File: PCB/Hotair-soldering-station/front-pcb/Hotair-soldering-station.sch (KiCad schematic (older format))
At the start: 54 parts, among them J1 fan_reg_pot, J2 main-board-conn, J3 hot_on, J4 solder_on, Q1 BC817, Q10 BC807, Q11 BC807, Q12 BC807, Q13 BC807, Q14 BC807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

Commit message: add heater controll circuit, add sch block structure
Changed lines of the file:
@@
 U 1 1 5FAAAC4E
 P 5550 8125
-F 0 "R6" H 5480 8079 50  0000 R CNN
-F 1 "5k6" H 5480 8170 50  0000 R CNN
+F 0 "R6" V 5650 8175 50  0000 R CNN
+F 1 "5k6" V 5450 8200 50  0000 R CNN
 F 2 "Capacitors:0805" V 5480 8125 50  0001 C CNN
 F 3 "~" H 5550 8125 50  0001 C CNN

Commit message: main schematic update, front pcb routing
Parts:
- SW1: value SW_Push -> HOTAIR_UP
- SW2: value SW_Push -> HOTAIR_DOWN
- SW3: value SW_Push -> SIRON_UP
- SW4: value SW_Push -> SIRON_DOWN
- U3, U4: symbol My-Lib:3-dig-7-seg-display-common-anode -> Hotair-soldering-station-rescue:3-dig-7-seg-display-common-anode-My-Lib
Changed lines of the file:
@@
 P 12125 5725
 F 0 "SW1" H 11925 5775 50  0000 C CNN
-F 1 "SW_Push" H 12125 5919 50  0001 C CNN
+F 1 "HOTAIR_UP" H 12125 5919 50  0001 C CNN
 F 2 "My-Footprints:push_button_12mm" H 12125 5925 50  0001 C CNN
 F 3 "~" H 12125 5925 50  0001 C CNN
@@
 P 12125 5925
 F 0 "SW2" H 11925 5975 50  0000 C CNN
-F 1 "SW_Push" H 12125 6119 50  0001 C CNN
+F 1 "HOTAIR_DOWN" H 12125 6119 50  0001 C CNN
 F 2 "My-Footprints:push_button_12mm" H 12125 6125 50  0001 C CNN
 F 3 "~" H 12125 6125 50  0001 C CNN
@@
 P 12175 7125
 F 0 "SW3" H 11975 7175 50  0000 C CNN
-F 1 "SW_Push" H 12175 7319 50  0001 C CNN
+F 1 "SIRON_UP" H 12175 7319 50  0001 C CNN
 F 2 "My-Footprints:push_button_12mm" H 12175 7325 50  0001 C CNN
 F 3 "~" H 12175 7325 50  0001 C CNN
@@
 P 12175 7325
 F 0 "SW4" H 11975 7375 50  0000 C CNN
-F 1 "SW_Push" H 12175 7519 50  0001 C CNN
+F 1 "SIRON_DOWN" H 12175 7519 50  0001 C CNN
 F 2 "My-Footprints:push_button_12mm" H 12175 7525 50  0001 C CNN
 F 3 "~" H 12175 7525 50  0001 C CNN
@@
 	11425 4725 11425 8125
 $Comp
-L My-Lib:3-dig-7-seg-display-common-anode U4
+L Hotair-soldering-station-rescue:3-dig-7-seg-display-common-anode-My-Lib U4
 U 1 1 5F79E7AA
 P 8200 7975
@@
 	8950 5525 9650 5525
 $Comp
-L My-Lib:3-dig-7-seg-display-common-anode U3
+L Hotair-soldering-station-rescue:3-dig-7-seg-display-common-anode-My-Lib U3
 U 1 1 5F79D382
 P 8200 5475

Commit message: routing progress
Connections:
- net SEG_B: now reaches U1.1 (QB)
- net SEG_B: now also R7.1; no longer R2.1
- net SEG_A: now reaches U1.15 (QA)
- net SEG_A: now also R8.1; no longer R1.1
- net SEG_C: now reaches U1.2 (QC)
- net SEG_C: now also R6.1; no longer R3.1
- net SEG_D: now reaches U1.3 (QD)
- net SEG_D: now also R5.1; no longer R4.1
- net SEG_E: now reaches U1.4 (QE)
- net SEG_E: now also R4.1; no longer R5.1
- net HOTAIR_DIG3: now reaches U1.5 (QF)
- net HOTAIR_DIG3: now also R20.2; no longer R6.1
- net HOTAIR_DIG2: now reaches U1.6 (QG)
- net HOTAIR_DIG2: now also R19.2; no longer R7.1
- net HOTAIR_DIG1: now reaches U1.7 (QH)
- net HOTAIR_DIG1: now also R22.2; no longer R8.1
- net at U2.1 (QB): no longer R19.2
- net SEG_DP: now reaches U2.15 (QA)
- net SEG_DP: now also R1.1; no longer R20.2
- net SEG_G: now reaches U2.2 (QC)
- net SEG_G: now also R2.1; no longer R22.2
- net IRON_DIG1: now reaches U2.3 (QD)
- net IRON_DIG1: now also R21.2; no longer R18.2
- net IRON_DIG2: now reaches R17.2, U2.4 (QE)
- net IRON_DIG3: now reaches U2.5 (QF)
- net IRON_DIG3: now also R18.2; no longer R21.2
- new net SEG_F: R3.1
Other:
- moved on the sheet: R20, U1, U2

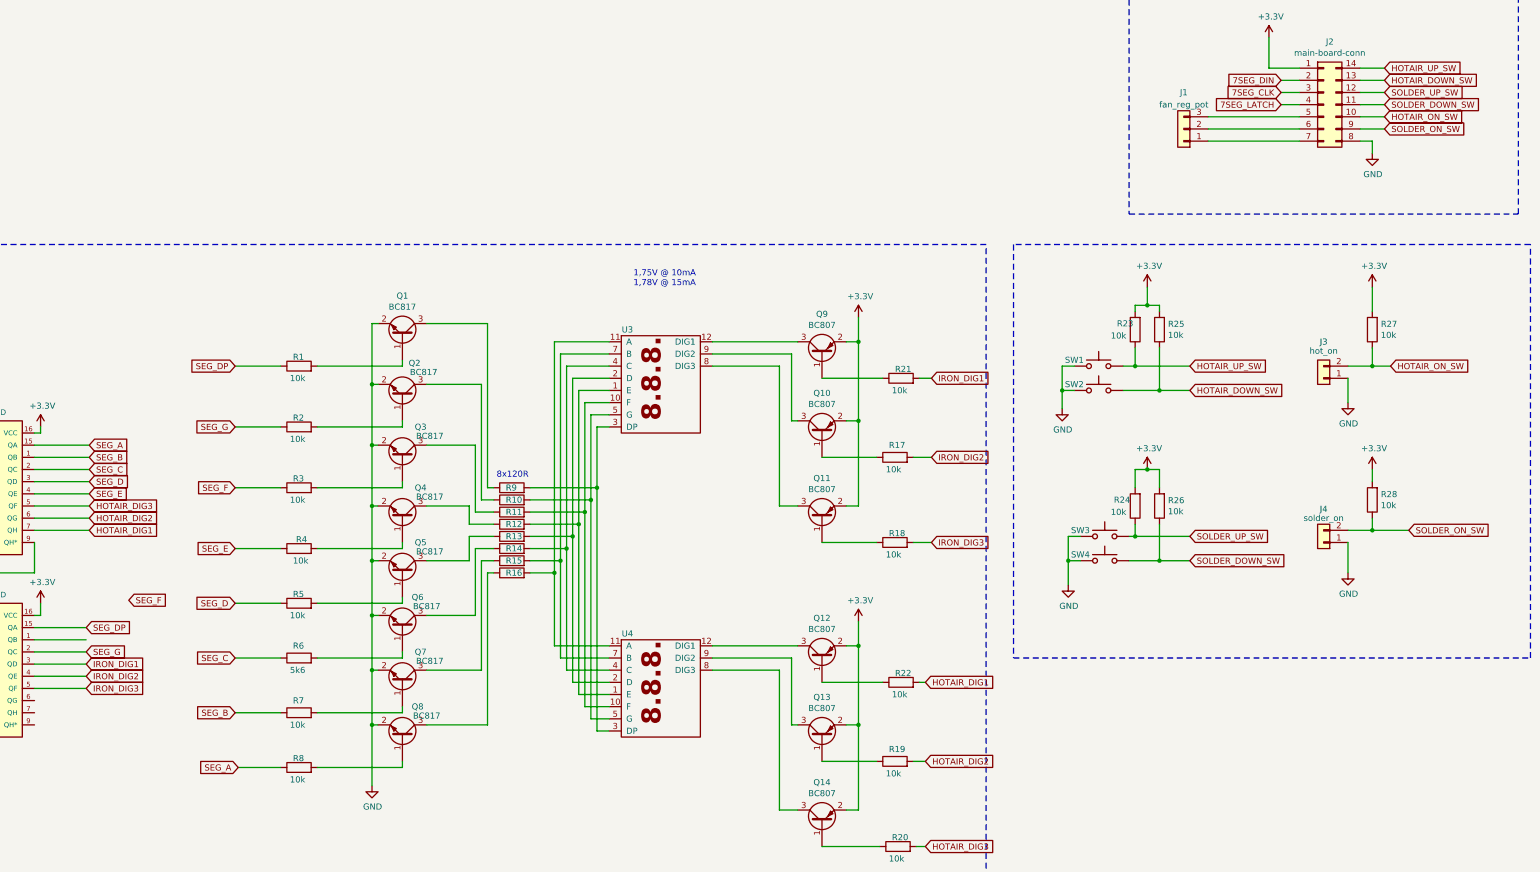
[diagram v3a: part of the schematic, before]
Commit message: add hot air fan buttons
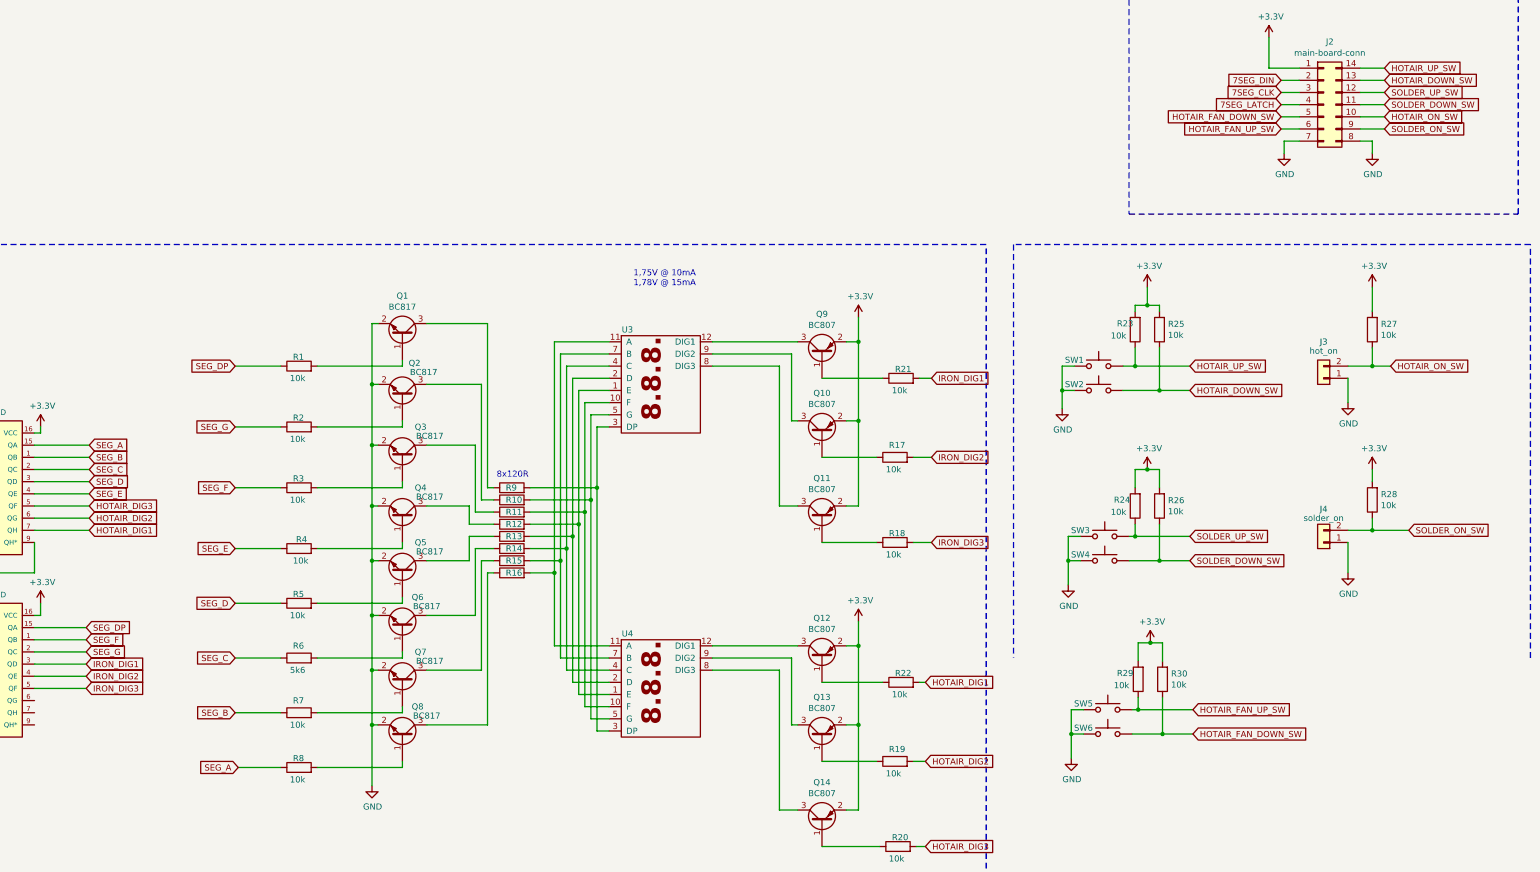
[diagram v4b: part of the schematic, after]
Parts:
- removed J1: fan_reg_pot, Connector_PinHeader_2.54mm:PinHeader_1x03_P2.54mm_Vertical, symbol Connector_Generic:Conn_01x03
- added R29, R30: 10k, Capacitors:0805, symbol Device:R
- added SW5: SIRON_UP, Switches:TACTILE_SWITCH_PTH_12MM, symbol Switch:SW_Push
- added SW6: SIRON_DOWN, Switches:TACTILE_SWITCH_PTH_12MM, symbol Switch:SW_Push
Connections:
- net +3V3: now also R29.2, R30.2
- net GND: now also J2.7 (Pin_7), SW5.1, SW6.1
- net SEG_F: now also U2.1 (QB)
- net HOTAIR_FAN_DOWN_SW: now reaches J2.5 (Pin_5)
- net HOTAIR_FAN_DOWN_SW: now also R30.1, SW6.2
- net HOTAIR_FAN_UP_SW: now reaches J2.6 (Pin_6)
- net HOTAIR_FAN_UP_SW: now also R29.1, SW5.2
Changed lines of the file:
@@
 SOLDER_ON_SW
-Wire Notes Line
-	11425 8125 15675 8125
 Wire Notes Line
 	15675 8125 15675 4725
@@
 Wire Wire Line
 	14275 3775 14475 3775
-$Comp
-L Connector_Generic:Conn_01x03 J1
-U 1 1 5F94CEDF
-P 12825 3775
-F 0 "J1" H 12825 3475 50  0000 C CNN
-F 1 "fan_reg_pot" H 12825 3575 50  0000 C CNN
-F 2 "Connector_PinHeader_2.54mm:PinHeader_1x03_P2.54mm_Vertical" H 12825 3775 50  0001 C CNN
-F 3 "~" H 12825 3775 50  0001 C CNN
-	1    12825 3775
-	-1   0    0    1
-$EndComp
-Wire Wire Line
-	13025 3675 13775 3675
-Wire Wire Line
-	13775 3775 13025 3775
-Wire Wire Line
-	13775 3875 13025 3875
 Wire Notes Line
 	12375 2475 12375 4475
@@
 Text GLabel 3825 6775 2    50   Input ~ 0
 SEG_E
-Text GLabel 4150 7650 2    50   Input ~ 0
+Text GLabel 3800 7975 2    50   Input ~ 0
 SEG_F
 Text GLabel 3800 8075 2    50   Input ~ 0
@@
 Text GLabel 10750 7175 2    50   Input ~ 0
 IRON_DIG3
+$Comp
+L Switch:SW_Push SW5
+U 1 1 5F8FF5F0
+P 12200 8550
+F 0 "SW5" H 12000 8600 50  0000 C CNN
+F 1 "SIRON_UP" H 12200 8744 50  0001 C CNN
+F 2 "Switches:TACTILE_SWITCH_PTH_12MM" H 12200 8750 50  0001 C CNN
+F 3 "~" H 12200 8750 50  0001 C CNN
+	1    12200 8550
+	1    0    0    -1
+$EndComp
+$Comp
+L Switch:SW_Push SW6
+U 1 1 5F8FF5F6
+P 12200 8750
+F 0 "SW6" H 12000 8800 50  0000 C CNN
+F 1 "SIRON_DOWN" H 12200 8944 50  0001 C CNN
+F 2 "Switches:TACTILE_SWITCH_PTH_12MM" H 12200 8950 50  0001 C CNN
+F 3 "~" H 12200 8950 50  0001 C CNN
+	1    12200 8750
+	1    0    0    -1
+$EndComp
+$Comp
+L power:GND #PWR0117
+U 1 1 5F8FF5FC
+P 11900 8950
+F 0 "#PWR0117" H 11900 8700 50  0001 C CNN
+F 1 "GND" H 11905 8777 50  0000 C CNN
+F 2 "" H 11900 8950 50  0001 C CNN
+F 3 "" H 11900 8950 50  0001 C CNN
+	1    11900 8950
+	1    0    0    -1
+$EndComp
+Wire Wire Line
+	12000 8750 11900 8750
+Wire Wire Line
+	11900 8750 11900 8950
+Wire Wire Line
+	12000 8550 11900 8550
+Wire Wire Line
+	11900 8550 11900 8750
+Connection ~ 11900 8750
+$Comp
+L Device:R R29
+U 1 1 5F8FF607
+P 12450 8300
+F 0 "R29" H 12625 8250 50  0000 R CNN
+F 1 "10k" H 12650 8350 50  0000 R CNN
+F 2 "Capacitors:0805" V 12380 8300 50  0001 C CNN
+F 3 "~" H 12450 8300 50  0001 C CNN
+	1    12450 8300
+	-1   0    0    1
+$EndComp
+$Comp
+L Device:R R30
+U 1 1 5F8FF60D
+P 12650 8300
+F 0 "R30" H 12580 8254 50  0000 R CNN
+F 1 "10k" H 12580 8345 50  0000 R CNN
+F 2 "Capacitors:0805" V 12580 8300 50  0001 C CNN
+F 3 "~" H 12650 8300 50  0001 C CNN
+	1    12650 8300
+	-1   0    0    1
+$EndComp
+Wire Wire Line
+	12400 8550 12450 8550
+Wire Wire Line
+	12450 8550 12450 8450
+Wire Wire Line
+	12400 8750 12650 8750
+Wire Wire Line
+	12650 8750 12650 8450
+$Comp
+L power:+3.3V #PWR0118
+U 1 1 5F8FF617
+P 12550 8000
+F 0 "#PWR0118" H 12550 7850 50  0001 C CNN
+F 1 "+3.3V" H 12565 8173 50  0000 C CNN
+F 2 "" H 12550 8000 50  0001 C CNN
+F 3 "" H 12550 8000 50  0001 C CNN
+	1    12550 8000
+	1    0    0    -1
+$EndComp
+Wire Wire Line
+	12450 8150 12450 8000
+Wire Wire Line
+	12450 8000 12550 8000
+Wire Wire Line
+	12550 8000 12650 8000
+Wire Wire Line
+	12650 8000 12650 8150
+Connection ~ 12550 8000
+Text GLabel 12900 8550 2    50   Input ~ 0
+HOTAIR_FAN_UP_SW
+Wire Wire Line
+	12900 8550 12450 8550
+Connection ~ 12450 8550
+Text GLabel 12900 8750 2    50   Input ~ 0
+HOTAIR_FAN_DOWN_SW
+Wire Wire Line
+	12900 8750 12650 8750
+Connection ~ 12650 8750
+Text GLabel 13625 3775 0    50   Input ~ 0
+HOTAIR_FAN_UP_SW
+Text GLabel 13625 3675 0    50   Input ~ 0
+HOTAIR_FAN_DOWN_SW
+Wire Wire Line
+	13775 3675 13625 3675
+Wire Wire Line
+	13775 3775 13625 3775
+$Comp
+L power:GND #PWR0119
+U 1 1 5F953902
+P 13650 3975
+F 0 "#PWR0119" H 13650 3725 50  0001 C CNN
+F 1 "GND" H 13655 3802 50  0000 C CNN
+F 2 "" H 13650 3975 50  0001 C CNN
+F 3 "" H 13650 3975 50  0001 C CNN
+	1    13650 3975
+	1    0    0    -1
+$EndComp
+Wire Wire Line
+	13650 3975 13650 3875
+Wire Wire Line
+	13650 3875 13775 3875
 $EndSCHEMATC
